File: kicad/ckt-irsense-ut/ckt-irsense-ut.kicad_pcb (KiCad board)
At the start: 2 copper layers, 25.4 x 15 mm, 14 parts, among them J1 SM04B-SRSS, J2 AVR-ISP, Q1 SSM6N357R, U1 AP7381-33Y, U2 TMD2672, U3 ATtiny13A-SS

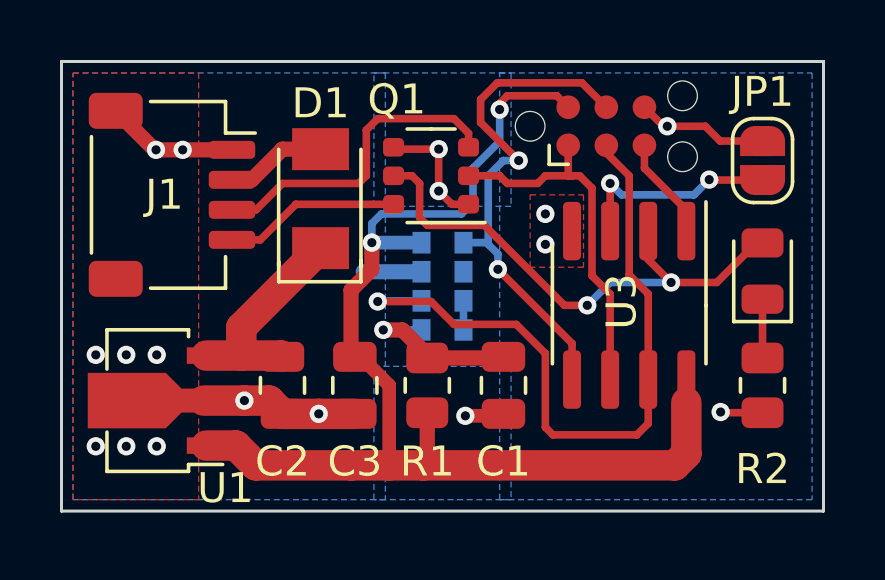
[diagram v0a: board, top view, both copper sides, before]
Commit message: Update to add text
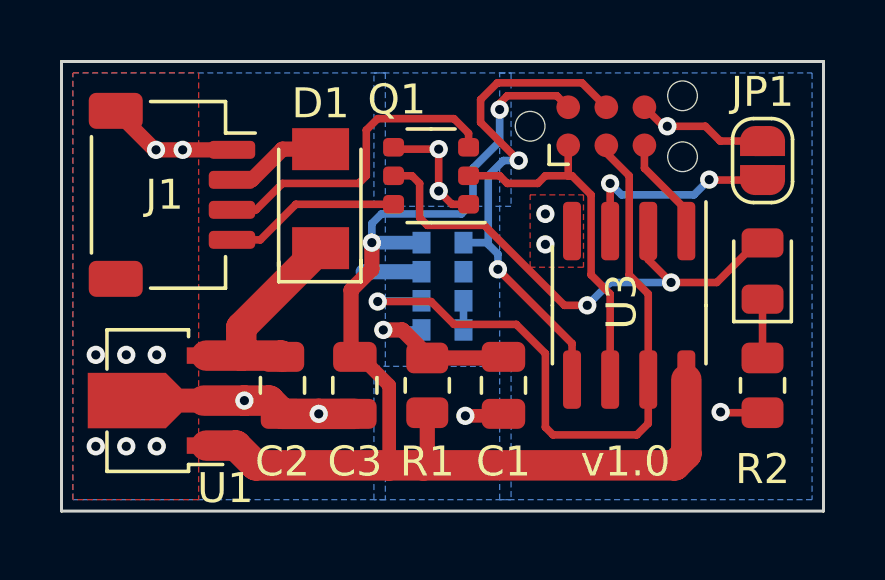
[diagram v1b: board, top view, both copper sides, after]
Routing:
- net GND: track 23.6 -> 22.8 mm
- net Net-(C3-Pad1): track 40.9 -> 41.5 mm
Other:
- board text added: "CKT-IRSENSE-UT v1.0"
- board text added: "Iowa Scaled Engineering"
- board text added: "v1.0"
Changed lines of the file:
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@@
   (net 8 "Net-(J1-Pad4)")
   (net 9 "Net-(J2-Pad1)")
-  (net 10 "Net-(J2-Pad2)")
+  (net 10 "Net-(C3-Pad1)")
   (net 11 "Net-(J2-Pad3)")
   (net 12 "Net-(J2-Pad4)")
@@
       (net 9 "Net-(J2-Pad1)") (pinfunction "MISO") (pintype "output"))
     (pad "2" connect circle (at -1.27 -0.635) (size 0.7874 0.7874) (layers "F.Cu" "F.Mask")
-      (net 10 "Net-(J2-Pad2)") (pinfunction "VCC") (pintype "power_in"))
+      (net 10 "Net-(C3-Pad1)") (pinfunction "VCC") (pintype "power_in"))
     (pad "3" connect circle (at 0 0.635) (size 0.7874 0.7874) (layers "F.Cu" "F.Mask")
       (net 11 "Net-(J2-Pad3)") (pinfunction "SCK") (pintype "input"))
@@
       (net 11 "Net-(J2-Pad3)") (pinfunction "PB2") (pintype "bidirectional"))
     (pad "8" smd roundrect (at 2.475 -1.905 270) (size 1.95 0.6) (layers "F.Cu" "F.Paste" "F.Mask") (roundrect_rratio 0.25)
-      (net 10 "Net-(J2-Pad2)") (pinfunction "VCC") (pintype "power_in"))
+      (net 10 "Net-(C3-Pad1)") (pinfunction "VCC") (pintype "power_in"))
     (model "${KICAD6_3DMODEL_DIR}/Package_SO.3dshapes/SOIC-8_3.9x4.9mm_P1.27mm.wrl"
       (offset (xyz 0 0 0))
@@
     (fp_line (start -1 0.625) (end -1 -0.625) (layer "F.Fab") (width 0.1))
     (pad "1" smd roundrect (at -0.95 0 270) (size 1 1.45) (layers "F.Cu" "F.Paste" "F.Mask") (roundrect_rratio 0.25)
-      (net 10 "Net-(J2-Pad2)") (pintype "passive"))
+      (net 10 "Net-(C3-Pad1)") (pintype "passive"))
     (pad "2" smd roundrect (at 0.95 0 270) (size 1 1.45) (layers "F.Cu" "F.Paste" "F.Mask") (roundrect_rratio 0.25)
       (net 2 "GND") (pintype "passive"))
@@
     (fp_line (start -0.95 2.25) (end -0.95 -1.25) (layer "F.Fab") (width 0.1))
     (pad "1" smd rect (at -1.65 -1.5 180) (size 1.3 0.55) (layers "F.Cu" "F.Paste" "F.Mask")
-      (net 10 "Net-(J2-Pad2)") (pinfunction "VO") (pintype "power_out"))
+      (net 10 "Net-(C3-Pad1)") (pinfunction "VO") (pintype "power_out"))
     (pad "2" smd custom (at -1.5625 0 180) (size 1.475 0.8) (layers "F.Cu" "F.Paste" "F.Mask")
       (net 2 "GND") (pinfunction "GND") (pintype "power_in") (zone_connect 2)
@@
       (net 1 "Net-(C1-Pad1)") (pintype "passive"))
     (pad "2" smd roundrect (at 0.9125 0 270) (size 1.025 1.4) (layers "F.Cu" "F.Paste" "F.Mask") (roundrect_rratio 0.243902)
-      (net 10 "Net-(J2-Pad2)") (pintype "passive"))
+      (net 10 "Net-(C3-Pad1)") (pintype "passive"))
     (model "${KICAD6_3DMODEL_DIR}/Resistor_SMD.3dshapes/R_0805_2012Metric.wrl"
       (offset (xyz 0 0 0))
@@
     (property "Sheetname" "")
     (attr smd)
-    (fp_text reference "U2" (at -3.81 -0.127 270 unlocked) (layer "B.SilkS")
+    (fp_text reference "U2" (at 3.048 -1.524 unlocked) (layer "B.SilkS")
       (effects (font (size 1 1) (thickness 0.15)) (justify mirror))
     )
@@
       (net 2 "GND") (pinfunction "GND") (pintype "power_in"))
     (pad "4" smd rect locked (at 1.455 -0.7 90) (size 0.72 0.6) (layers "B.Cu" "B.Paste" "B.Mask")
-      (net 10 "Net-(J2-Pad2)") (pinfunction "LEDA") (pintype "bidirectional"))
+      (net 10 "Net-(C3-Pad1)") (pinfunction "LEDA") (pintype "bidirectional"))
     (pad "5" smd rect locked (at -1.455 0.7 90) (size 0.72 0.6) (layers "B.Cu" "B.Paste" "B.Mask")
       (net 16 "Net-(U2-Pad5)") (pinfunction "LEDK") (pintype "bidirectional"))
@@
   )
   (gr_rect (start 25.4 176.784) (end 50.8 191.77) (layer "Edge.Cuts") (width 0.1) (fill none))
+  (gr_text "Iowa Scaled Engineering" (at 41.148 187.198) (layer "B.SilkS")
+    (effects (font (size 1 1) (thickness 0.15)) (justify mirror))
+  )
+  (gr_text "CKT-IRSENSE-UT\nv1.0 " (at 32.766 179.07) (layer "B.SilkS")
+    (effects (font (size 1 1) (thickness 0.15)) (justify mirror))
+  )
+  (gr_text "v1.0" (at 44.196 190.119) (layer "F.SilkS")
+    (effects (font (size 1 1) (thickness 0.15)))
+  )
   (gr_text "Q3" (at 59.944 200.914) (layer "F.Fab")
     (effects (font (size 0.32 0.32) (thickness 0.05)))
@@
   (segment (start 47.3945 188.4915) (end 47.371 188.468) (width 0.254) (layer "F.Cu") (net 2))
   (segment (start 38.862 188.595) (end 40.066 188.595) (width 0.4572) (layer "F.Cu") (net 2))
-  (segment (start 33.086 188.529) (end 32.766 188.529) (width 0.508) (layer "F.Cu") (net 2))
   (segment (start 29.44 179.729) (end 28.551 179.729) (width 0.508) (layer "F.Cu") (net 2))
   (segment (start 45.466 178.943) (end 44.831 178.308) (width 0.254) (layer "F.Cu") (net 2))
-  (segment (start 35.626 188.529) (end 35.179 188.529) (width 0.4572) (layer "F.Cu") (net 2))
   (segment (start 37.973 179.705) (end 37.973 181.102) (width 0.254) (layer "F.Cu") (net 2))
   (segment (start 37.973 179.705) (end 36.53 179.705) (width 0.254) (layer "F.Cu") (net 2))
@@
   (segment (start 30.225 186.587) (end 31.393 186.587) (width 1.016) (layer "F.Cu") (net 3))
   (segment (start 31.393 186.587) (end 32.724 186.587) (width 1.016) (layer "F.Cu") (net 3))
-  (segment (start 30.267 186.629) (end 30.225 186.587) (width 0.508) (layer "F.Cu") (net 3))
   (segment (start 32.724 186.587) (end 32.766 186.629) (width 1.016) (layer "F.Cu") (net 3))
   (segment (start 31.083 180.729) (end 31.742 180.729) (width 0.508) (layer "F.Cu") (net 4))
@@
   (segment (start 32.028 182.729) (end 31.083 182.729) (width 0.254) (layer "F.Cu") (net 8))
   (segment (start 33.213 181.544) (end 32.028 182.729) (width 0.254) (layer "F.Cu") (net 8))
-  (segment (start 42.672 180.594) (end 42.418 180.594) (width 0.254) (layer "F.Cu") (net 9))
+  (segment (start 43.053 183.896) (end 43.053 181.229) (width 0.254) (layer "F.Cu") (net 9))
   (segment (start 42.291 179.578) (end 42.291 180.594) (width 0.254) (layer "F.Cu") (net 9))
   (segment (start 41.275 180.848) (end 41.529 180.594) (width 0.254) (layer "F.Cu") (net 9))
-  (segment (start 43.688 184.531) (end 43.0832 183.9262) (width 0.254) (layer "F.Cu") (net 9))
+  (segment (start 43.688 184.531) (end 43.053 183.896) (width 0.254) (layer "F.Cu") (net 9))
+  (segment (start 43.688 187.387) (end 43.688 184.531) (width 0.254) (layer "F.Cu") (net 9))
   (segment (start 41.529 180.594) (end 42.418 180.594) (width 0.254) (layer "F.Cu") (net 9))
   (segment (start 42.418 180.594) (end 42.291 180.594) (width 0.254) (layer "F.Cu") (net 9))
-  (segment (start 43.688 187.387) (end 43.688 184.531) (width 0.254) (layer "F.Cu") (net 9))
-  (segment (start 43.0832 181.0052) (end 42.672 180.594) (width 0.254) (layer "F.Cu") (net 9))
+  (segment (start 43.053 181.229) (end 42.418 180.594) (width 0.254) (layer "F.Cu") (net 9))
   (segment (start 40.259 180.848) (end 41.275 180.848) (width 0.254) (layer "F.Cu") (net 9))
-  (segment (start 43.0832 183.9262) (end 43.0832 181.0052) (width 0.254) (layer "F.Cu") (net 9))
   (segment (start 40.005 180.594) (end 40.259 180.848) (width 0.254) (layer "F.Cu") (net 9))
   (segment (start 38.969 180.594) (end 40.005 180.594) (width 0.254) (layer "F.Cu") (net 9))
@@
   (segment (start 35.372 186.629) (end 36.322 187.579) (width 0.4572) (layer "F.Cu") (net 10))
   (segment (start 35.052 186.502) (end 35.179 186.629) (width 0.508) (layer "F.Cu") (net 10))
+  (segment (start 46.228 189.865) (end 46.228 187.387) (width 1.016) (layer "F.Cu") (net 10))
+  (segment (start 45.847 190.246) (end 46.228 189.865) (width 1.016) (layer "F.Cu") (net 10))
   (segment (start 35.3435 186.629) (end 35.306 186.6665) (width 0.254) (layer "F.Cu") (net 10))
   (segment (start 36.322 187.579) (end 36.322 190.246) (width 0.4572) (layer "F.Cu") (net 10))
@@
   (segment (start 40.005 178.3842) (end 40.005 178.181) (width 0.254) (layer "F.Cu") (net 10))
   (segment (start 41.91 177.927) (end 42.291 178.308) (width 0.254) (layer "F.Cu") (net 10))
-  (segment (start 35.052 190.246) (end 36.322 190.246) (width 1.016) (layer "F.Cu") (net 10))
-  (segment (start 35.179 190.119) (end 35.052 190.246) (width 0.508) (layer "F.Cu") (net 10))
   (segment (start 31.218 189.587) (end 31.877 190.246) (width 1.016) (layer "F.Cu") (net 10))
   (segment (start 37.592 188.4915) (end 37.592 190.119) (width 0.508) (layer "F.Cu") (net 10))
-  (segment (start 45.847 190.246) (end 46.228 189.865) (width 1.016) (layer "F.Cu") (net 10))
-  (segment (start 46.228 189.865) (end 46.228 188.149) (width 1.016) (layer "F.Cu") (net 10))
   (segment (start 35.052 184.404) (end 35.052 186.502) (width 0.508) (layer "F.Cu") (net 10))
   (segment (start 36.322 190.246) (end 37.465 190.246) (width 1.016) (layer "F.Cu") (net 10))
-  (segment (start 31.877 190.246) (end 35.052 190.246) (width 1.016) (layer "F.Cu") (net 10))
+  (segment (start 31.877 190.246) (end 36.322 190.246) (width 1.016) (layer "F.Cu") (net 10))
+  (segment (start 37.465 190.246) (end 45.847 190.246) (width 1.016) (layer "F.Cu") (net 10))
   (segment (start 35.179 186.629) (end 35.372 186.629) (width 0.4572) (layer "F.Cu") (net 10))
   (segment (start 30.225 189.587) (end 31.218 189.587) (width 1.016) (layer "F.Cu") (net 10))
-  (segment (start 37.465 190.246) (end 45.847 190.246) (width 1.016) (layer "F.Cu") (net 10))
   (via (at 40.005 178.3842) (size 0.6096) (drill 0.3048) (layers "F.Cu" "B.Cu") (net 10))
   (via (at 35.745 182.822) (size 0.6096) (drill 0.3048) (layers "F.Cu" "B.Cu") (net 10))
